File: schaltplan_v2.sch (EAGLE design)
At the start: 43 parts, among them T1 2N3565, T2 2N3565, T3 2N3565, T4 2N3565, T5 2N3565, T6 2N3565, T7 2N3565, T8 2N3565

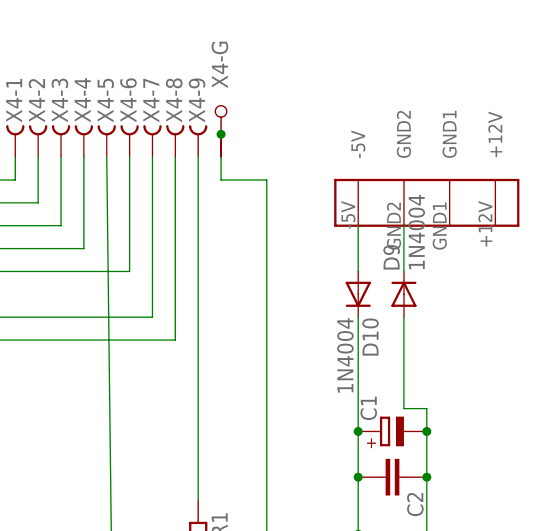
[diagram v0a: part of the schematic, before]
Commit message: fixed ground areas
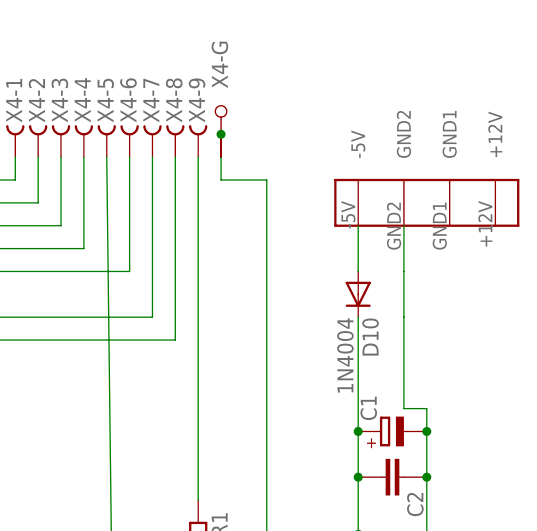
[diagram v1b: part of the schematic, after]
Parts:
- removed D9: 1N4004, diode:1N4004
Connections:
- net N$1 renamed GND2
- removed net N$19: C1.-, C2.1, D9.A, T1.C, T2.C, T3.C, T4.C, T5.C, T6.C, T7.C, T8.C, X4-G.G1
- removed net N$9: D9.C, U$14.GND2
- new net GND: C1.-, C2.1, T1.C, T2.C, T3.C, T4.C, T5.C, T6.C, T7.C, T8.C, U$14.GND2, X4-G.G1
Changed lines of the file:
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@@
 <grid distance="0.1" unitdist="inch" unit="inch" style="lines" multiple="1" display="no" altdistance="0.01" altunitdist="inch" altunit="inch"/>
 <layers>
-<layer number="1" name="Top" color="4" fill="1" visible="yes" active="no"/>
-<layer number="16" name="Bottom" color="1" fill="1" visible="yes" active="no"/>
-<layer number="17" name="Pads" color="2" fill="1" visible="yes" active="no"/>
-<layer number="18" name="Vias" color="2" fill="1" visible="yes" active="no"/>
-<layer number="19" name="Unrouted" color="6" fill="1" visible="yes" active="no"/>
-<layer number="20" name="Dimension" color="15" fill="1" visible="yes" active="no"/>
-<layer number="21" name="tPlace" color="7" fill="1" visible="yes" active="no"/>
-<layer number="22" name="bPlace" color="7" fill="1" visible="yes" active="no"/>
-<layer number="23" name="tOrigins" color="15" fill="1" visible="yes" active="no"/>
-<layer number="24" name="bOrigins" color="15" fill="1" visible="yes" active="no"/>
-<layer number="25" name="tNames" color="7" fill="1" visible="yes" active="no"/>
-<layer number="26" name="bNames" color="7" fill="1" visible="yes" active="no"/>
-<layer number="27" name="tValues" color="7" fill="1" visible="yes" active="no"/>
-<layer number="28" name="bValues" color="7" fill="1" visible="yes" active="no"/>
+<layer number="1" name="Top" color="4" fill="1" visible="no" active="no"/>
+<layer number="16" name="Bottom" color="1" fill="1" visible="no" active="no"/>
+<layer number="17" name="Pads" color="2" fill="1" visible="no" active="no"/>
+<layer number="18" name="Vias" color="2" fill="1" visible="no" active="no"/>
+<layer number="19" name="Unrouted" color="6" fill="1" visible="no" active="no"/>
+<layer number="20" name="Dimension" color="15" fill="1" visible="no" active="no"/>
+<layer number="21" name="tPlace" color="7" fill="1" visible="no" active="no"/>
+<layer number="22" name="bPlace" color="7" fill="1" visible="no" active="no"/>
+<layer number="23" name="tOrigins" color="15" fill="1" visible="no" active="no"/>
+<layer number="24" name="bOrigins" color="15" fill="1" visible="no" active="no"/>
+<layer number="25" name="tNames" color="7" fill="1" visible="no" active="no"/>
+<layer number="26" name="bNames" color="7" fill="1" visible="no" active="no"/>
+<layer number="27" name="tValues" color="7" fill="1" visible="no" active="no"/>
+<layer number="28" name="bValues" color="7" fill="1" visible="no" active="no"/>
 <layer number="29" name="tStop" color="7" fill="3" visible="no" active="no"/>
 <layer number="30" name="bStop" color="7" fill="6" visible="no" active="no"/>
@@
 <layer number="35" name="tGlue" color="7" fill="4" visible="no" active="no"/>
 <layer number="36" name="bGlue" color="7" fill="5" visible="no" active="no"/>
-<layer number="37" name="tTest" color="7" fill="1" visible="yes" active="no"/>
-<layer number="38" name="bTest" color="7" fill="1" visible="yes" active="no"/>
+<layer number="37" name="tTest" color="7" fill="1" visible="no" active="no"/>
+<layer number="38" name="bTest" color="7" fill="1" visible="no" active="no"/>
 <layer number="39" name="tKeepout" color="4" fill="11" visible="no" active="no"/>
 <layer number="40" name="bKeepout" color="1" fill="11" visible="no" active="no"/>
@@
 <layer number="44" name="Drills" color="7" fill="1" visible="no" active="no"/>
 <layer number="45" name="Holes" color="7" fill="1" visible="no" active="no"/>
-<layer number="46" name="Milling" color="3" fill="1" visible="yes" active="no"/>
-<layer number="47" name="Measures" color="7" fill="1" visible="yes" active="no"/>
-<layer number="48" name="Document" color="7" fill="1" visible="yes" active="no"/>
-<layer number="49" name="Reference" color="7" fill="1" visible="yes" active="no"/>
-<layer number="51" name="tDocu" color="7" fill="1" visible="yes" active="no"/>
-<layer number="52" name="bDocu" color="7" fill="1" visible="yes" active="no"/>
+<layer number="46" name="Milling" color="3" fill="1" visible="no" active="no"/>
+<layer number="47" name="Measures" color="7" fill="1" visible="no" active="no"/>
+<layer number="48" name="Document" color="7" fill="1" visible="no" active="no"/>
+<layer number="49" name="Reference" color="7" fill="1" visible="no" active="no"/>
+<layer number="51" name="tDocu" color="7" fill="1" visible="no" active="no"/>
+<layer number="52" name="bDocu" color="7" fill="1" visible="no" active="no"/>
 <layer number="91" name="Nets" color="2" fill="1" visible="yes" active="yes"/>
 <layer number="92" name="Busses" color="1" fill="1" visible="yes" active="yes"/>
@@
 <part name="T7" library="transistor" deviceset="2N3565" device=""/>
 <part name="T8" library="transistor" deviceset="2N3565" device=""/>
-<part name="D9" library="diode" deviceset="1N4004" device=""/>
 <part name="D10" library="diode" deviceset="1N4004" device=""/>
 <part name="C1" library="rcl" deviceset="CPOL-EU" device="E3.5-8"/>
@@
 <instance part="T7" gate="G$1" x="-27.94" y="-96.52" rot="R270"/>
 <instance part="T8" gate="G$1" x="-53.34" y="-96.52" rot="R270"/>
-<instance part="D9" gate="1" x="198.12" y="-58.42" rot="R90"/>
 <instance part="D10" gate="1" x="193.04" y="-58.42" rot="R270"/>
 <instance part="C1" gate="G$1" x="195.58" y="-73.66" rot="R90"/>
@@
 </busses>
 <nets>
-<net name="N$1" class="0">
+<net name="GND2" class="0">
 <segment>
 <wire x1="195.58" y1="-147.32" x2="132.08" y2="-147.32" width="0.1524" layer="91"/>
@@
 </segment>
 </net>
-<net name="N$19" class="0">
+<net name="GND" class="0">
 <segment>
 <pinref part="C2" gate="G$1" pin="1"/>
@@
 <junction x="-7.62" y="-86.36"/>
 <wire x1="182.88" y1="-99.06" x2="182.88" y2="-86.36" width="0.1524" layer="91"/>
-<pinref part="D9" gate="1" pin="A"/>
 <wire x1="198.12" y1="-60.96" x2="198.12" y2="-71.12" width="0.1524" layer="91"/>
 <wire x1="198.12" y1="-71.12" x2="200.66" y2="-71.12" width="0.1524" layer="91"/>
@@
 <pinref part="X4" gate="-G" pin="G1"/>
 <wire x1="177.8" y1="-45.72" x2="177.8" y2="-43.18" width="0.1524" layer="91"/>
+<pinref part="U$14" gate="G$1" pin="GND2"/>
+<wire x1="198.12" y1="-50.8" x2="198.12" y2="-55.88" width="0.1524" layer="91"/>
+<wire x1="198.12" y1="-60.96" x2="198.12" y2="-55.88" width="0.1524" layer="91"/>
 </segment>
 </net>
@@
 </segment>
 </net>
-<net name="N$9" class="0">
-<segment>
-<pinref part="U$14" gate="G$1" pin="GND2"/>
-<pinref part="D9" gate="1" pin="C"/>
-<wire x1="198.12" y1="-50.8" x2="198.12" y2="-55.88" width="0.1524" layer="91"/>
-</segment>
-</net>

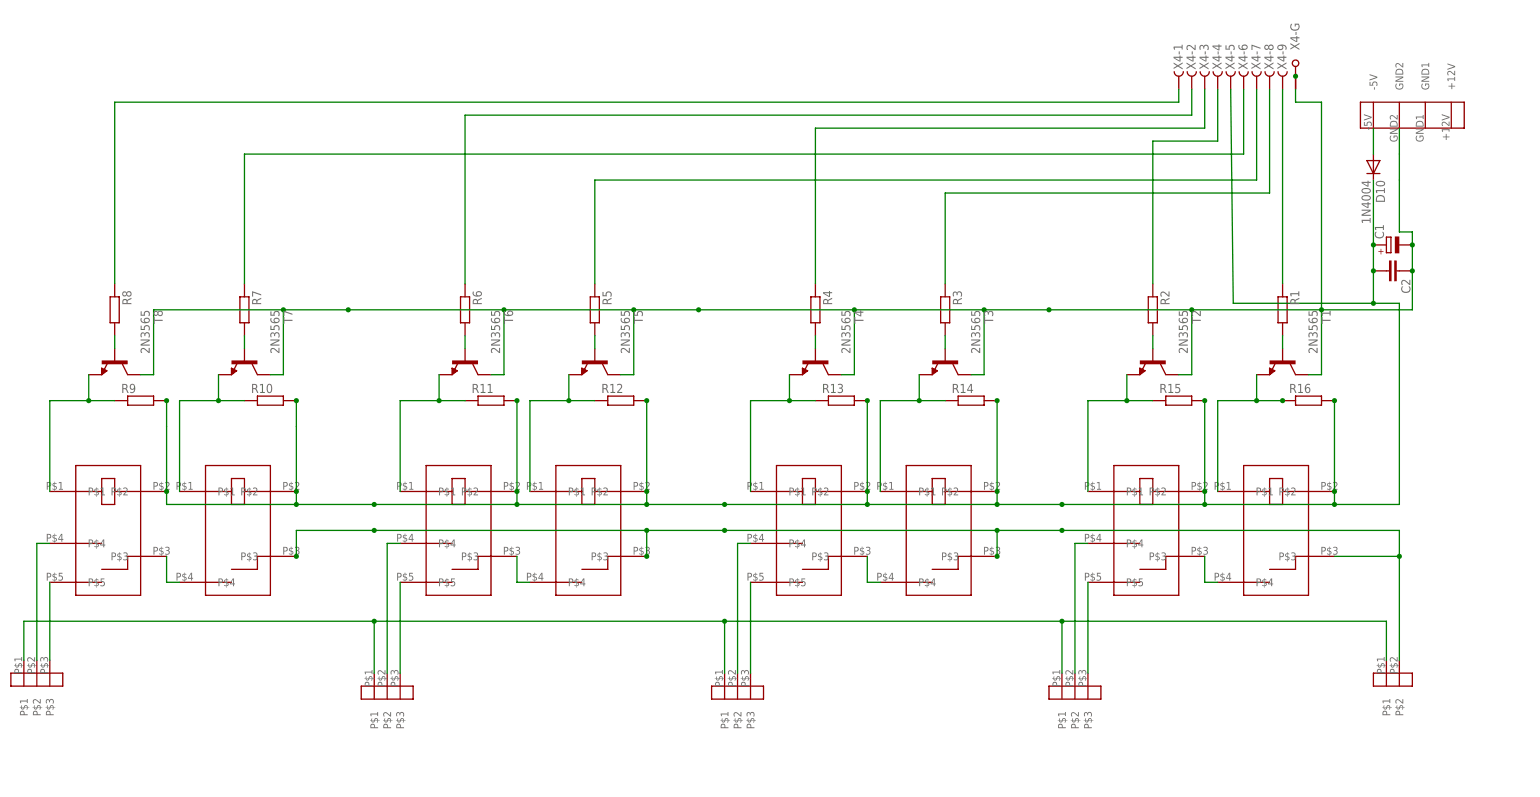
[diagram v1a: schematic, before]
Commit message: minor layout fixes
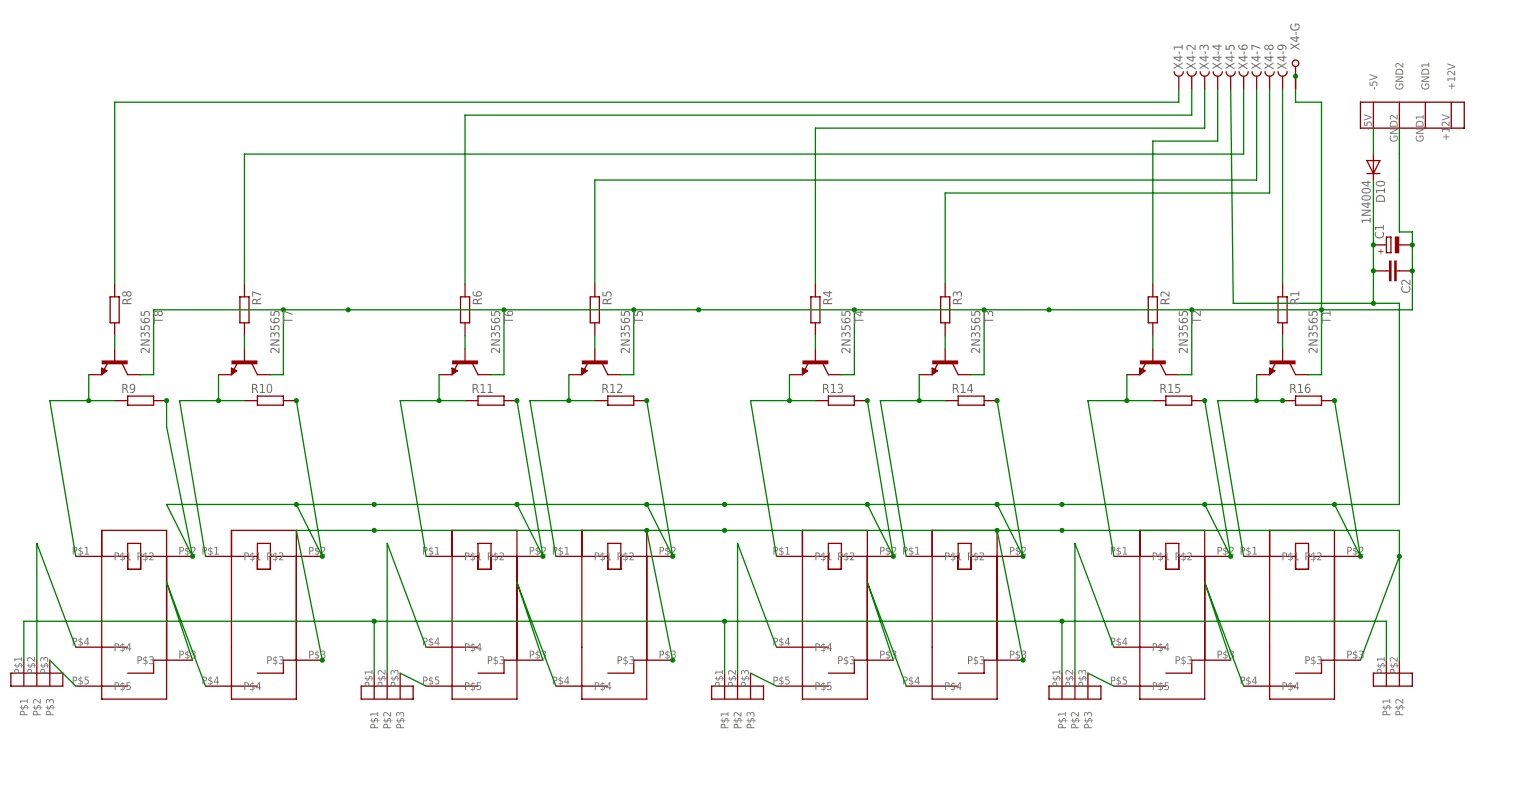
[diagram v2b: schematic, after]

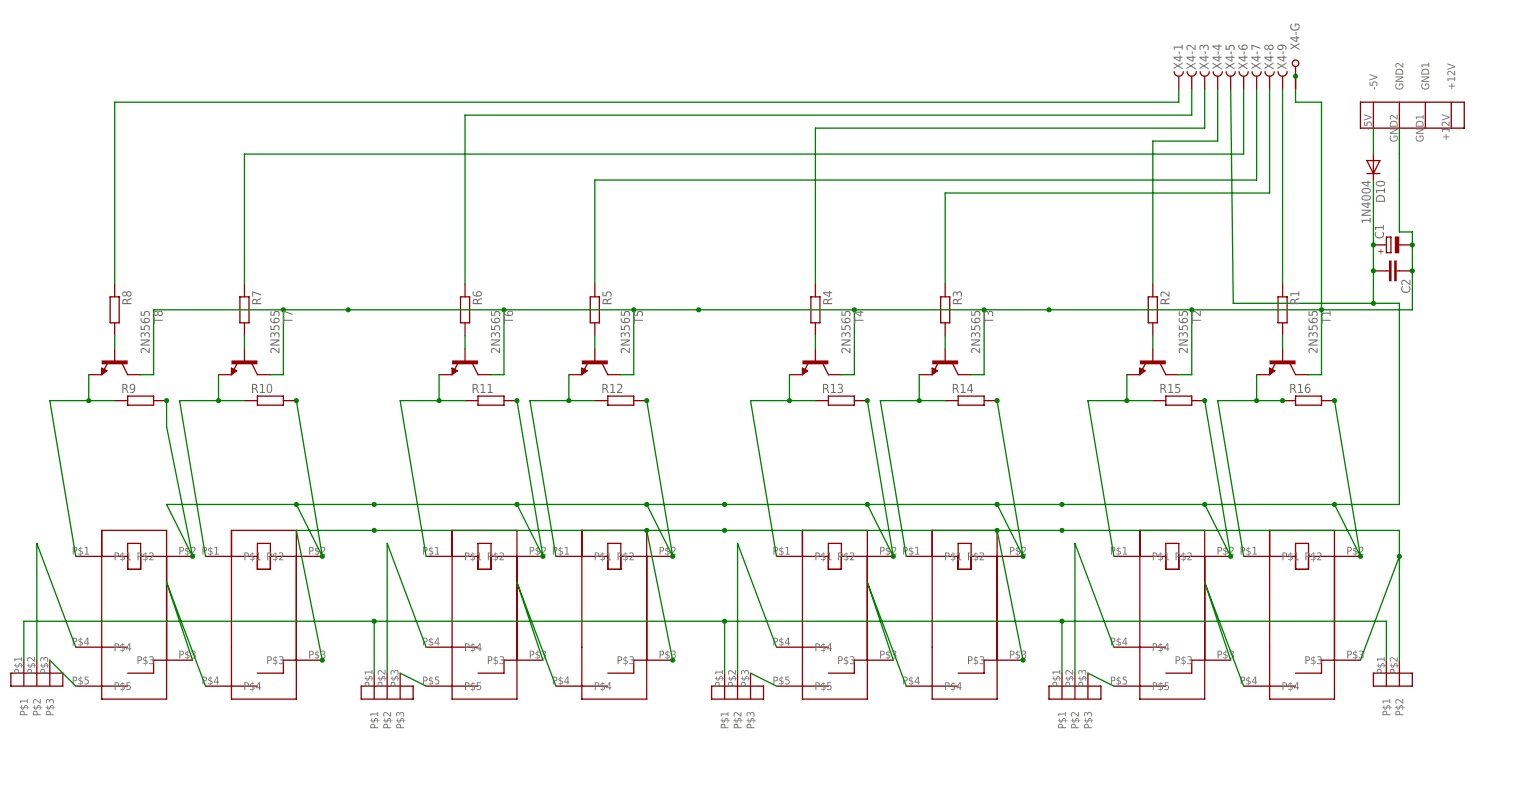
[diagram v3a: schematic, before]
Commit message: fix ERC issues and schematic, reroute some signals
overall connection was lost due to some signal renamings, some parts
were not connected at all. additionally added restrict area around drill
holes
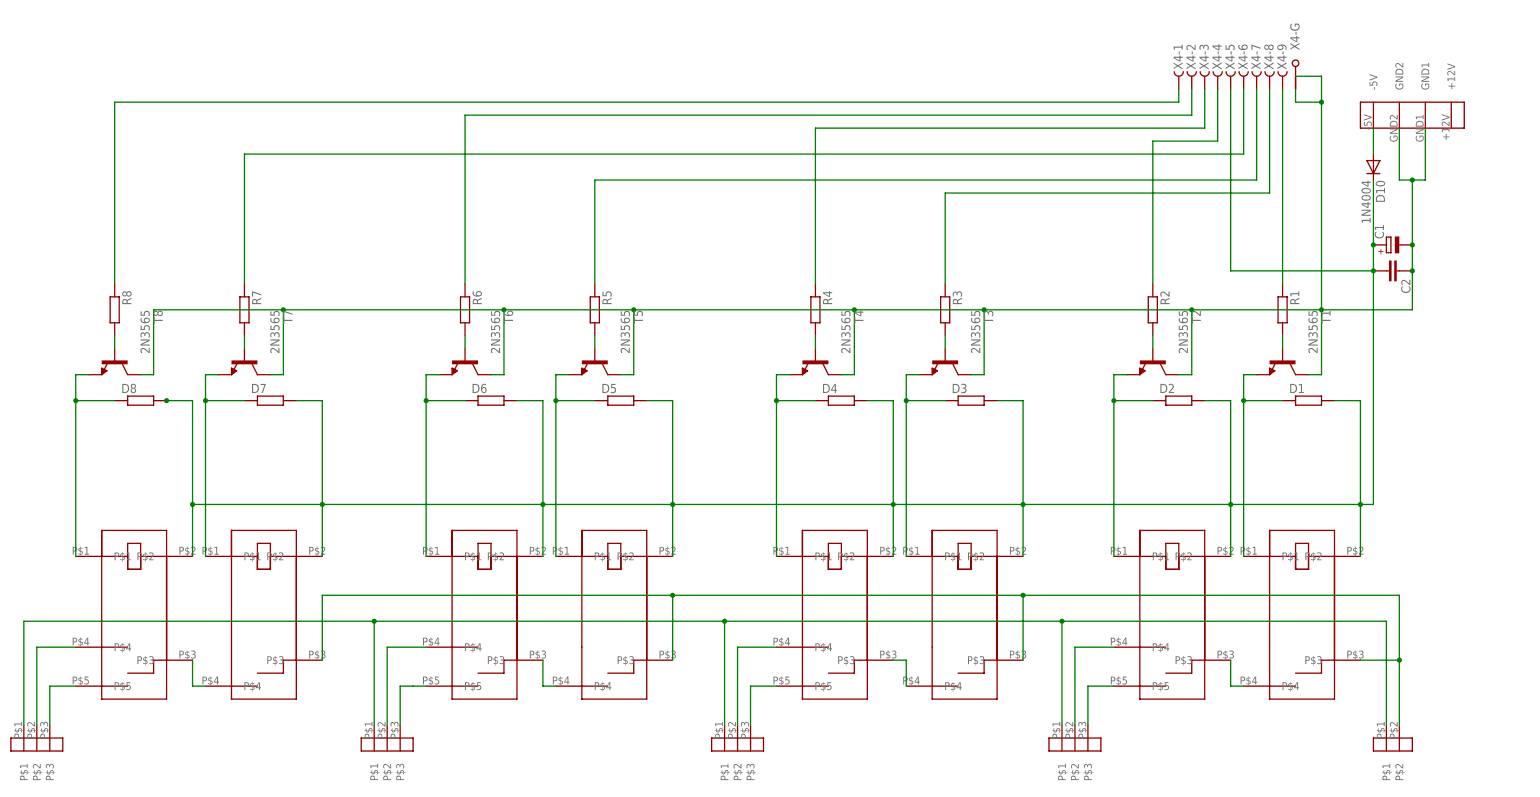
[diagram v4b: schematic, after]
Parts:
- renumbered R10 to D7, R11 to D6, R12 to D5, R13 to D4, R14 to D3, R15 to D2, R16 to D1, R9 to D8
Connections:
- removed net N$10: X4-G.G2
- net GND: now also U$14.GND1, X4-G.G2

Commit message: fix wrong connections in schematics
transitor pins were connected wrong and resistors are not diodes!
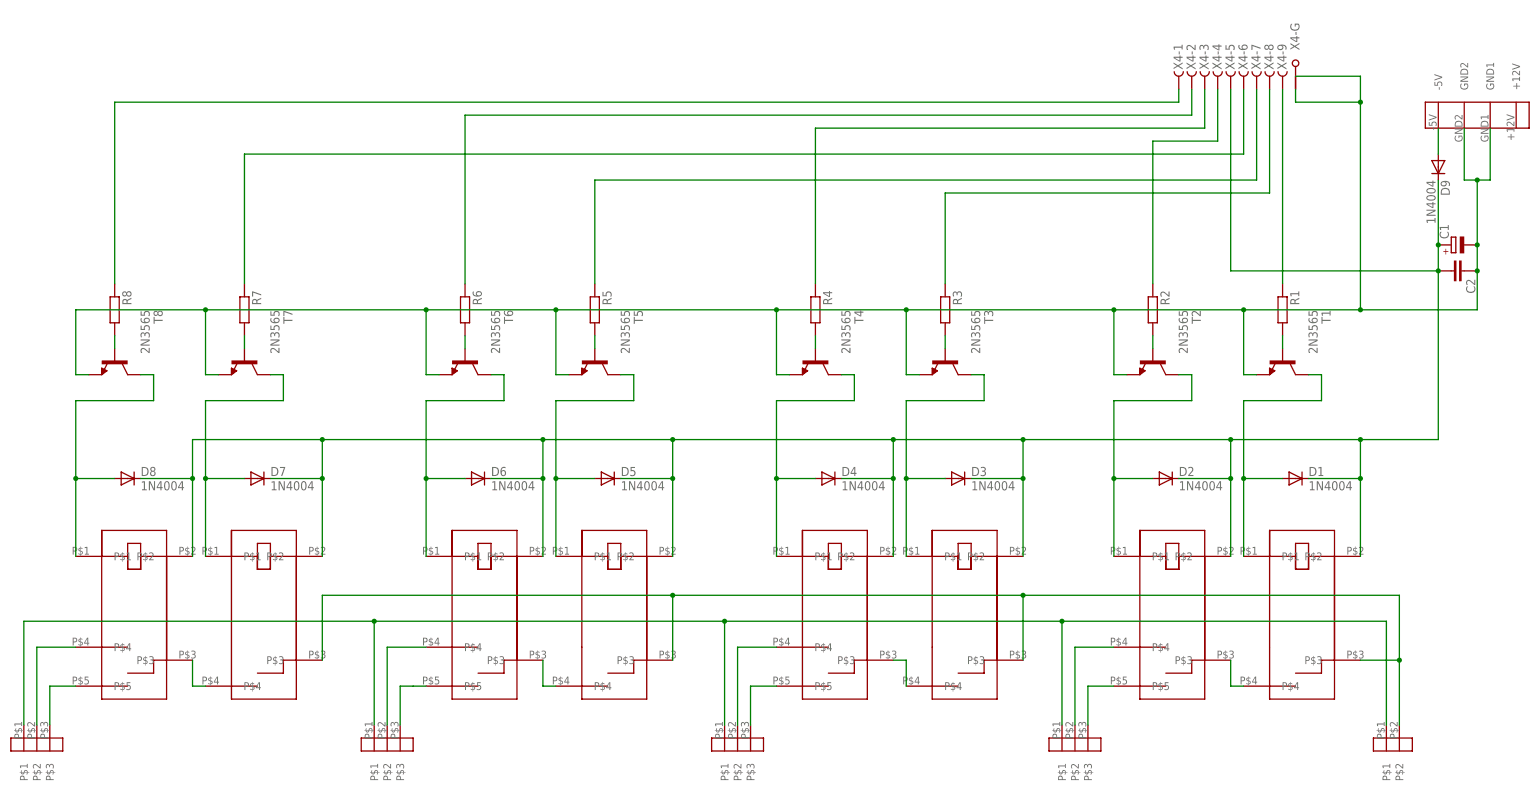
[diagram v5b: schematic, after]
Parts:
- removed D10: 1N4004, diode:1N4004
- added D9: 1N4004, diode:1N4004
- D1, D2, D3, D4, D5, D6, D7, D8: value (none) -> 1N4004; device rcl:R-EU_0207/2V -> diode:1N4004
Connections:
- removed net N$20: D3.1, T3.E, U$3.P$1
- removed net N$25: D4.1, T4.E, U$4.P$1
- removed net N$39: D6.1, T6.E, U$6.P$1
- removed net N$46: D7.1, T7.E, U$7.P$1
- removed net N$51: D8.1, T8.E, U$8.P$1
- new net N$10: D2.A, T2.C, U$2.P$1
- new net N$19: D4.A, T4.C, U$4.P$1
- new net N$33: D6.A, T6.C, U$6.P$1
- new net N$35: D8.A, T8.C, U$8.P$1
- new net V+: C1.+, C2.2, D1.C, D2.C, D3.C, D4.C, D5.C, D6.C, D7.C, D8.C, D9.C, U$1.P$2, U$2.P$2, U$3.P$2, U$4.P$2, U$5.P$2, U$6.P$2, U$7.P$2, U$8.P$2, X4-5.F
- net GND: now also T1.E, T2.E, T3.E, T4.E, T5.E, T6.E, T7.E, T8.E; no longer T1.C, T2.C, T3.C, T4.C, T5.C, T6.C, T7.C, T8.C
- net N$12: now also D3.A, T3.C, U$3.P$1; no longer D2.1, T2.E, U$2.P$1
- net N$24: now also D5.A, T5.C, U$5.P$1; no longer C1.+, C2.2, D1.2, D10.C, D2.2, D3.2, D4.2, D5.2, D6.2, D7.2, D8.2, U$1.P$2, U$2.P$2, U$3.P$2, U$4.P$2, U$5.P$2, U$6.P$2, U$7.P$2, U$8.P$2, X4-5.F
- net N$34: now also D7.A, T7.C, U$7.P$1; no longer D5.1, T5.E, U$5.P$1
- net N$6: now also D1.A, T1.C; no longer D1.1, T1.E
- net N$7: now also D9.A; no longer D10.A
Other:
- moved on the sheet: C1, C2
